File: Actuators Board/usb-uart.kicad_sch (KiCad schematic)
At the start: 16 parts, among them U3 INTERFACE-CP2102-GMR(QFN28)

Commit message: Preliminary layout of buck converter components
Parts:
- D10: footprint Diode_SMD:D_0805_2012Metric_Castellated -> Diode_SMD:D_0805_2012Metric
- D5: renamed from D?; footprint LED_SMD:LED_0603_1608Metric_Castellated -> LED_SMD:LED_0603_1608Metric
- gave numbers to parts that had none: 4
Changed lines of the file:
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@@
     (effects (font (size 1.27 1.27)) (justify left))
   )
-  (symbol (lib_id "power:GND") (at 127 96.52 90)
-    (in_bom yes) (on_board yes)
-    (property "Reference" "#PWR?" (id 0) (at 133.35 96.52 0)
+  (symbol (lib_id "power:GND") (at 127 96.52 90) (unit 1)
+    (in_bom yes) (on_board yes)
+    (property "Reference" "#PWR0119" (id 0) (at 133.35 96.52 0)
       (effects (font (size 1.27 1.27)) hide)
     )
@@
     (pin "1")
   )
-  (symbol (lib_id "Device:R_Small") (at 123.19 99.06 270)
-    (in_bom yes) (on_board yes)
-    (property "Reference" "R?" (id 0) (at 123.19 94.0816 90))
+  (symbol (lib_id "Device:R_Small") (at 123.19 99.06 270) (unit 1)
+    (in_bom yes) (on_board yes)
+    (property "Reference" "R16" (id 0) (at 123.19 94.0816 90))
     (property "Value" "5.1k" (id 1) (at 123.19 96.393 90))
     (property "Footprint" "Resistor_SMD:R_0603_1608Metric" (id 2) (at 123.19 99.06 0)
@@
     (pin "2")
   )
-  (symbol (lib_id "Device:R_Small") (at 123.19 93.98 90)
-    (in_bom yes) (on_board yes)
-    (property "Reference" "R?" (id 0) (at 123.19 89.0016 90))
+  (symbol (lib_id "Device:R_Small") (at 123.19 93.98 90) (unit 1)
+    (in_bom yes) (on_board yes)
+    (property "Reference" "R15" (id 0) (at 123.19 89.0016 90))
     (property "Value" "5.1k" (id 1) (at 123.19 91.313 90))
     (property "Footprint" "Resistor_SMD:R_0603_1608Metric" (id 2) (at 123.19 93.98 0)
@@
     (pin "2")
   )
-  (symbol (lib_id "power:GND") (at 96.52 130.81 0)
-    (in_bom yes) (on_board yes)
-    (property "Reference" "#PWR?" (id 0) (at 96.52 137.16 0)
+  (symbol (lib_id "power:GND") (at 96.52 130.81 0) (unit 1)
+    (in_bom yes) (on_board yes)
+    (property "Reference" "#PWR0120" (id 0) (at 96.52 137.16 0)
       (effects (font (size 1.27 1.27)) hide)
     )
@@
     (pin "1")
   )
-  (symbol (lib_id "Connector:USB_C_Receptacle_USB2.0") (at 100.33 104.14 0)
-    (in_bom yes) (on_board yes)
-    (property "Reference" "J?" (id 0) (at 103.0478 82.1182 0))
+  (symbol (lib_id "Connector:USB_C_Receptacle_USB2.0") (at 100.33 104.14 0) (unit 1)
+    (in_bom yes) (on_board yes)
+    (property "Reference" "J3" (id 0) (at 103.0478 82.1182 0))
     (property "Value" "USB_C_Receptacle_USB2.0" (id 1) (at 103.0478 84.4296 0))
     (property "Footprint" "Connector_USB:USB_C_Receptacle_GCT_USB4085" (id 2) (at 104.14 104.14 0)
@@
     (pin "S1")
   )
-  (symbol (lib_id "power:GND") (at 132.08 144.78 0)
-    (in_bom yes) (on_board yes)
-    (property "Reference" "#PWR?" (id 0) (at 132.08 151.13 0)
+  (symbol (lib_id "power:GND") (at 132.08 144.78 0) (unit 1)
+    (in_bom yes) (on_board yes)
+    (property "Reference" "#PWR0121" (id 0) (at 132.08 151.13 0)
       (effects (font (size 1.27 1.27)) hide)
     )
@@
     (pin "1")
   )
-  (symbol (lib_id "Power_Protection:SP0503BAHT") (at 132.08 139.7 0)
-    (in_bom yes) (on_board yes)
-    (property "Reference" "D?" (id 0) (at 137.287 138.5316 0)
+  (symbol (lib_id "Power_Protection:SP0503BAHT") (at 132.08 139.7 0) (unit 1)
+    (in_bom yes) (on_board yes)
+    (property "Reference" "D4" (id 0) (at 137.287 138.5316 0)
       (effects (font (size 1.27 1.27)) (justify left))
     )
@@
     (pin "2")
   )
-  (symbol (lib_id "power:+3.3V") (at 137.16 74.93 180)
-    (in_bom yes) (on_board yes)
-    (property "Reference" "#PWR?" (id 0) (at 137.16 71.12 0)
+  (symbol (lib_id "power:+3.3V") (at 137.16 74.93 180) (unit 1)
+    (in_bom yes) (on_board yes)
+    (property "Reference" "#PWR0127" (id 0) (at 137.16 71.12 0)
       (effects (font (size 1.27 1.27)) hide)
     )
@@
     (pin "1")
   )
-  (symbol (lib_id "Device:LED_Small") (at 162.56 92.71 180)
-    (in_bom yes) (on_board yes)
-    (property "Reference" "D?" (id 0) (at 162.56 87.503 0))
+  (symbol (lib_id "Device:LED_Small") (at 162.56 92.71 180) (unit 1)
+    (in_bom yes) (on_board yes)
+    (property "Reference" "D5" (id 0) (at 162.56 87.503 0))
     (property "Value" "USB_LED" (id 1) (at 162.56 89.8144 0))
-    (property "Footprint" "LED_SMD:LED_0603_1608Metric_Castellated" (id 2) (at 162.56 92.71 90)
+    (property "Footprint" "LED_SMD:LED_0603_1608Metric" (id 2) (at 162.56 92.71 90)
       (effects (font (size 1.27 1.27)) hide)
     )
@@
     (pin "2")
   )
-  (symbol (lib_id "power:GND") (at 165.1 92.71 90)
-    (in_bom yes) (on_board yes)
-    (property "Reference" "#PWR?" (id 0) (at 171.45 92.71 0)
+  (symbol (lib_id "power:GND") (at 165.1 92.71 90) (unit 1)
+    (in_bom yes) (on_board yes)
+    (property "Reference" "#PWR0128" (id 0) (at 171.45 92.71 0)
       (effects (font (size 1.27 1.27)) hide)
     )
@@
     (property "Reference" "D10" (id 0) (at 91.44 46.8122 0))
     (property "Value" "D_Small" (id 1) (at 91.44 49.1236 0))
-    (property "Footprint" "Diode_SMD:D_0805_2012Metric_Castellated" (id 2) (at 91.44 52.07 90)
-      (effects (font (size 1.27 1.27)) hide)
-    )
+    (property "Footprint" "Diode_SMD:D_0805_2012Metric" (id 2) (at 91.44 52.07 90)
+      (effects (font (size 1.27 1.27)) hide)
+    )

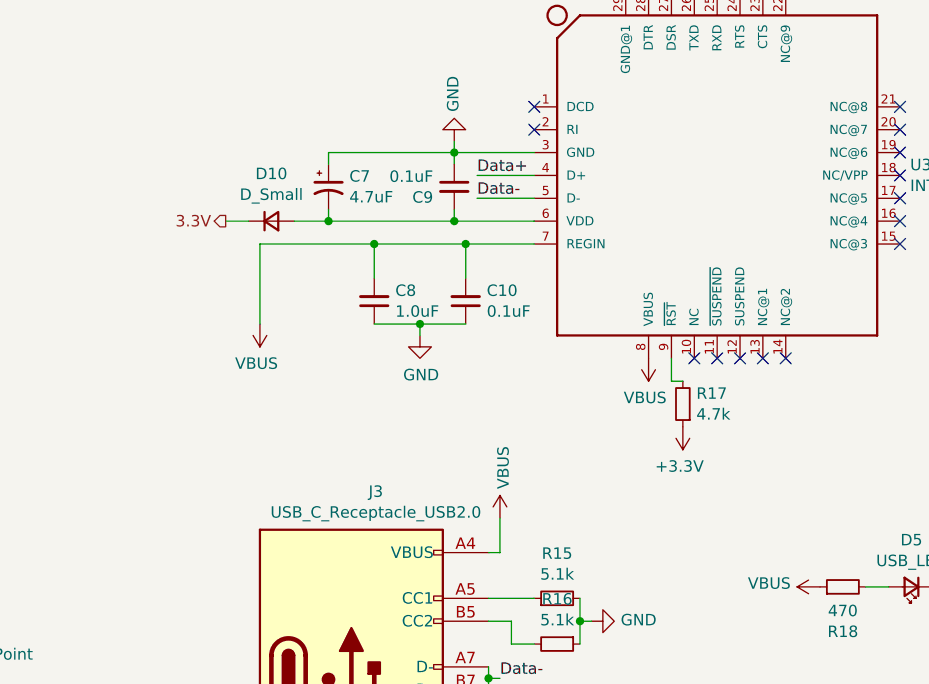
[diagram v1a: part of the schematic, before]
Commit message: Reconfigured uart converter to disable 5->3.3V regulation
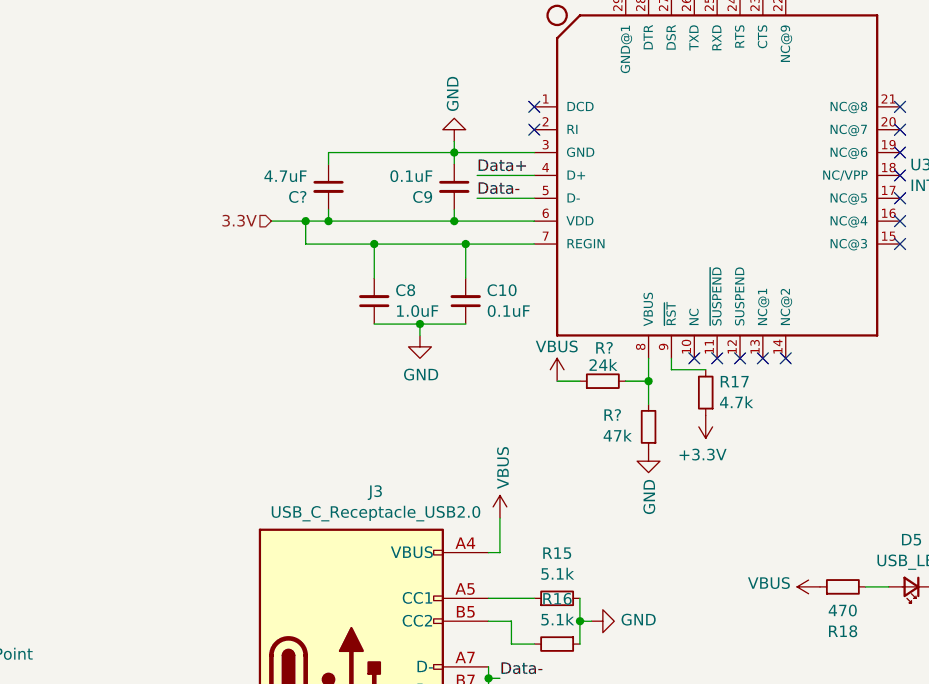
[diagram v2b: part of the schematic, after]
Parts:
- removed C7: 4.7uF, Capacitor_SMD:CP_Elec_3x5.3, symbol Device:CP1_Small
- removed D10: D_Small, Diode_SMD:D_0805_2012Metric, symbol Device:D_Small
- added C?: 4.7uF, Capacitor_SMD:C_0603_1608Metric, symbol Device:C_Small
- added R?: 47k, Resistor_SMD:R_0603_1608Metric, symbol Device:R_Small
- added R?: 24k, symbol Device:R_Small
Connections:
- net 3.3V: now also C10.2, C8.2, C9.2, U3.6 (VDD), U3.7 (REGIN), C?.2
- net GND: now also C?.1, R?.1
- net VBUS: now also R?.1; no longer C10.2, C8.2, U3.7 (REGIN), U3.8 (VBUS)
- new net: R?.2, R?.2, U3.8 (VBUS)
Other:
- moved on the sheet: R17

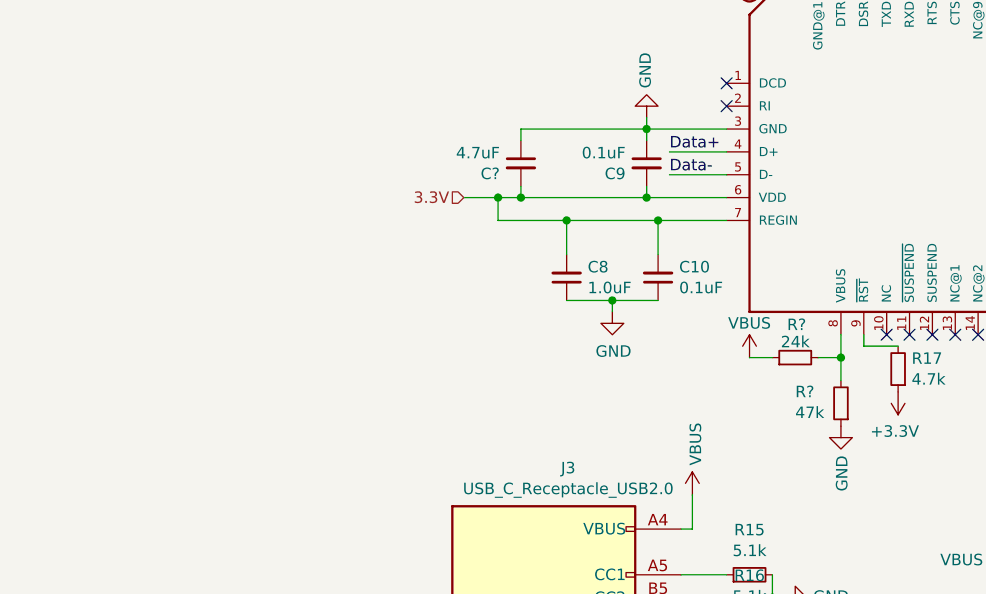
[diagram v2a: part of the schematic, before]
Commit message: Added LDO for 5 -> 3.3V
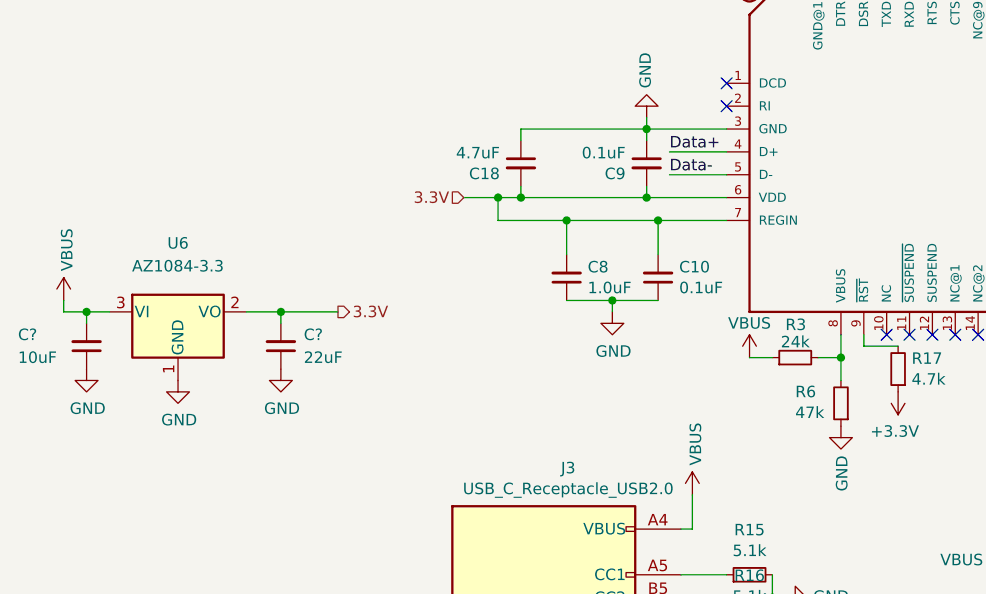
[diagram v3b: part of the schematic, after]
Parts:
- added C?: 10uF, symbol Device:C_Small
- added C?: 22uF, symbol Device:C_Small
- added U6: AZ1084-3.3, Package_TO_SOT_SMD:TO-252-3_TabPin2, symbol Regulator_Linear:AZ1084-3.3
- gave numbers to parts that had none: 3
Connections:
- net 3.3V: now also C?.2, U6.2 (VO)
- net GND: now also C?.1, C?.1, U6.1 (GND)
- net VBUS: now also C?.2, U6.3 (VI)
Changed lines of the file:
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@@
   (junction (at 95.25 52.07) (diameter 0) (color 0 0 0 0)
+  )
+  (junction (at 49.53 64.77) (diameter 0) (color 0 0 0 0)
+  )
+  (junction (at 71.12 64.77) (diameter 0) (color 0 0 0 0)
   )
   (junction (at 102.87 54.61) (diameter 0) (color 0 0 0 0)
@@
     (stroke (width 0) (type default) (color 0 0 0 0))
   )
+  (wire (pts (xy 67.31 64.77) (xy 71.12 64.77))
+    (stroke (width 0) (type default) (color 0 0 0 0))
+  )
   (wire (pts (xy 96.52 127) (xy 96.52 130.81))
     (stroke (width 0) (type default) (color 0 0 0 0))
@@
     (stroke (width 0) (type default) (color 0 0 0 0))
   )
+  (wire (pts (xy 46.99 63.5) (xy 46.99 64.77))
+    (stroke (width 0) (type default) (color 0 0 0 0))
+  )
   (wire (pts (xy 118.11 96.52) (xy 118.11 99.06))
     (stroke (width 0) (type default) (color 0 0 0 0))
@@
     (stroke (width 0) (type default) (color 0 0 0 0))
   )
+  (wire (pts (xy 71.12 64.77) (xy 71.12 66.04))
+    (stroke (width 0) (type default) (color 0 0 0 0))
+  )
   (wire (pts (xy 111.76 43.18) (xy 111.76 44.45))
     (stroke (width 0) (type default) (color 0 0 0 0))
@@
     (stroke (width 0) (type default) (color 0 0 0 0))
   )
+  (wire (pts (xy 49.53 64.77) (xy 52.07 64.77))
+    (stroke (width 0) (type default) (color 0 0 0 0))
+  )
   (wire (pts (xy 115.57 107.95) (xy 116.84 107.95))
     (stroke (width 0) (type default) (color 0 0 0 0))
   )
+  (wire (pts (xy 49.53 64.77) (xy 49.53 66.04))
+    (stroke (width 0) (type default) (color 0 0 0 0))
+  )
   (wire (pts (xy 116.84 88.9) (xy 115.57 88.9))
     (stroke (width 0) (type default) (color 0 0 0 0))
@@
     (stroke (width 0) (type default) (color 0 0 0 0))
   )
+  (wire (pts (xy 71.12 64.77) (xy 77.47 64.77))
+    (stroke (width 0) (type default) (color 0 0 0 0))
+  )
   (wire (pts (xy 44.45 99.06) (xy 52.07 99.06))
+    (stroke (width 0) (type default) (color 0 0 0 0))
+  )
+  (wire (pts (xy 46.99 64.77) (xy 49.53 64.77))
     (stroke (width 0) (type default) (color 0 0 0 0))
   )
@@
   )
   (hierarchical_label "DTR" (shape output) (at 133.35 19.05 90)
+    (effects (font (size 1.27 1.27)) (justify left))
+  )
+  (hierarchical_label "3.3V" (shape output) (at 77.47 64.77 0)
     (effects (font (size 1.27 1.27)) (justify left))
   )
@@
   (symbol (lib_id "Device:R_Small") (at 133.35 74.93 180) (unit 1)
     (in_bom yes) (on_board yes)
-    (property "Reference" "R?" (id 0) (at 128.27 73.66 0)
+    (property "Reference" "R6" (id 0) (at 128.27 73.66 0)
       (effects (font (size 1.27 1.27)) (justify right))
     )
@@
   (symbol (lib_id "Device:R_Small") (at 128.27 69.85 90) (unit 1)
     (in_bom yes) (on_board yes)
-    (property "Reference" "R?" (id 0) (at 129.4928 66.2004 90)
+    (property "Reference" "R3" (id 0) (at 129.4928 66.2004 90)
       (effects (font (size 1.27 1.27)) (justify left))
     )
@@
     (pin "2")
   )
+  (symbol (lib_id "power:GND") (at 71.12 71.12 0) (unit 1)
+    (in_bom yes) (on_board yes)
+    (property "Reference" "#PWR?" (id 0) (at 71.12 77.47 0)
+      (effects (font (size 1.27 1.27)) hide)
+    )
+    (property "Value" "GND" (id 1) (at 71.247 75.5142 0))
+    (property "Footprint" "" (id 2) (at 71.12 71.12 0)
+      (effects (font (size 1.27 1.27)) hide)
+    )
+    (property "Datasheet" "" (id 3) (at 71.12 71.12 0)
+      (effects (font (size 1.27 1.27)) hide)
+    )
+    (pin "1")
+  )
   (symbol (lib_id "power:VBUS") (at 123.19 69.85 0) (unit 1)
     (in_bom yes) (on_board yes)
-    (property "Reference" "#PWR?" (id 0) (at 123.19 73.66 0)
+    (property "Reference" "#PWR0111" (id 0) (at 123.19 73.66 0)
       (effects (font (size 1.27 1.27)) hide)
     )
@@
     (pin "1")
   )
+  (symbol (lib_id "Device:C_Small") (at 49.53 68.58 180) (unit 1)
+    (in_bom yes) (on_board yes)
+    (property "Reference" "C?" (id 0) (at 41.91 67.31 0)
+      (effects (font (size 1.27 1.27)) (justify right))
+    )
+    (property "Value" "10uF" (id 1) (at 41.91 69.85 0)
+      (effects (font (size 1.27 1.27)) (justify right))
+    )
+    (property "Footprint" "" (id 2) (at 49.53 68.58 0)
+      (effects (font (size 1.27 1.27)) hide)
+    )
+    (property "Datasheet" "~" (id 3) (at 49.53 68.58 0)
+      (effects (font (size 1.27 1.27)) hide)
+    )
+    (pin "1")
+    (pin "2")
+  )
+  (symbol (lib_id "Device:C_Small") (at 71.12 68.58 180) (unit 1)
+    (in_bom yes) (on_board yes)
+    (property "Reference" "C?" (id 0) (at 73.66 67.31 0)
+      (effects (font (size 1.27 1.27)) (justify right))
+    )
+    (property "Value" "22uF" (id 1) (at 73.66 69.85 0)
+      (effects (font (size 1.27 1.27)) (justify right))
+    )
+    (property "Footprint" "" (id 2) (at 71.12 68.58 0)
+      (effects (font (size 1.27 1.27)) hide)
+    )
+    (property "Datasheet" "~" (id 3) (at 71.12 68.58 0)
+      (effects (font (size 1.27 1.27)) hide)
+    )
+    (pin "1")
+    (pin "2")
+  )
+  (symbol (lib_id "Regulator_Linear:AZ1084-3.3") (at 59.69 64.77 0) (unit 1)
+    (in_bom yes) (on_board yes) (fields_autoplaced)
+    (property "Reference" "U6" (id 0) (at 59.69 57.15 0))
+    (property "Value" "AZ1084-3.3" (id 1) (at 59.69 59.69 0))
+    (property "Footprint" "Package_TO_SOT_SMD:TO-252-3_TabPin2" (id 2) (at 59.69 58.42 0)
+      (effects (font (size 1.27 1.27) italic) hide)
+    )
+    (property "Datasheet" "https://www.diodes.com/assets/Datasheets/AZ1084.pdf" (id 3) (at 59.69 64.77 0)
+      (effects (font (size 1.27 1.27)) hide)
+    )
+    (pin "1")
+    (pin "2")
+    (pin "3")
+  )
   (symbol (lib_id "power:GND") (at 133.35 77.47 0) (unit 1)
     (in_bom yes) (on_board yes)
-    (property "Reference" "#PWR?" (id 0) (at 133.35 83.82 0)
+    (property "Reference" "#PWR0137" (id 0) (at 133.35 83.82 0)
       (effects (font (size 1.27 1.27)) hide)
     )
@@
     (pin "1")
   )
+  (symbol (lib_id "power:VBUS") (at 46.99 63.5 0) (unit 1)
+    (in_bom yes) (on_board yes)
+    (property "Reference" "#PWR0123" (id 0) (at 46.99 67.31 0)
+      (effects (font (size 1.27 1.27)) hide)
+    )
+    (property "Value" "VBUS" (id 1) (at 47.371 60.2488 90)
+      (effects (font (size 1.27 1.27)) (justify left))
+    )
+    (property "Footprint" "" (id 2) (at 46.99 63.5 0)
+      (effects (font (size 1.27 1.27)) hide)
+    )
+    (property "Datasheet" "" (id 3) (at 46.99 63.5 0)
+      (effects (font (size 1.27 1.27)) hide)
+    )
+    (pin "1")
+  )
+  (symbol (lib_id "power:GND") (at 49.53 71.12 0) (unit 1)
+    (in_bom yes) (on_board yes)
+    (property "Reference" "#PWR?" (id 0) (at 49.53 77.47 0)
+      (effects (font (size 1.27 1.27)) hide)
+    )
+    (property "Value" "GND" (id 1) (at 49.657 75.5142 0))
+    (property "Footprint" "" (id 2) (at 49.53 71.12 0)
+      (effects (font (size 1.27 1.27)) hide)
+    )
+    (property "Datasheet" "" (id 3) (at 49.53 71.12 0)
+      (effects (font (size 1.27 1.27)) hide)
+    )
+    (pin "1")
+  )
+  (symbol (lib_id "power:GND") (at 59.69 72.39 0) (unit 1)
+    (in_bom yes) (on_board yes)
+    (property "Reference" "#PWR0126" (id 0) (at 59.69 78.74 0)
+      (effects (font (size 1.27 1.27)) hide)
+    )
+    (property "Value" "GND" (id 1) (at 59.817 76.7842 0))
+    (property "Footprint" "" (id 2) (at 59.69 72.39 0)
+      (effects (font (size 1.27 1.27)) hide)
+    )
+    (property "Datasheet" "" (id 3) (at 59.69 72.39 0)
+      (effects (font (size 1.27 1.27)) hide)
+    )
+    (pin "1")
+  )
   (symbol (lib_id "Device:C_Small") (at 97.79 48.26 0) (unit 1)
     (in_bom yes) (on_board yes)
-    (property "Reference" "C?" (id 0) (at 95.4532 49.4284 0)
-      (effects (font (size 1.27 1.27)) (justify right))
-    )
+    (property "Reference" "C18" (id 0) (at 95.4532 49.4284 0)
+      (effects (font (size 1.27 1.27)) (justify right))
+    )
